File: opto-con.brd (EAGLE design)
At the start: 13 x 8 mm, 2 parts

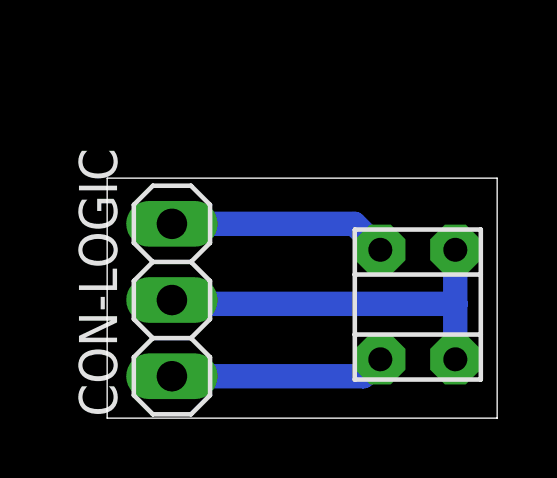
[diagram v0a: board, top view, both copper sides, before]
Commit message: Write meaning of measure signals to silkscreen.
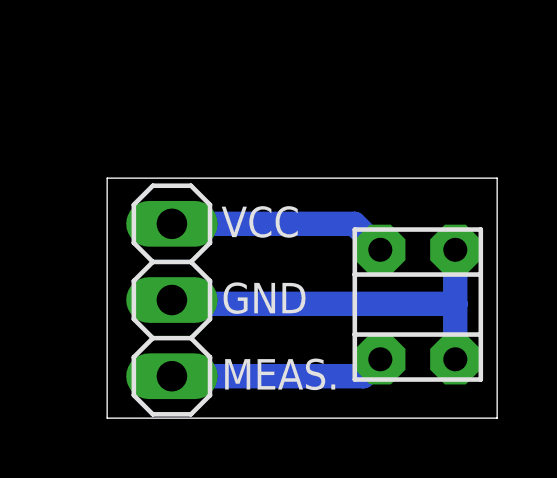
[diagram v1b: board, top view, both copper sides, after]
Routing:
- net GND: track 13.1 -> 13.7 mm
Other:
- board text added: "GND"
- board text added: "MEAS."
- board text added: "VCC"
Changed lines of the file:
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@@
 <grid distance="1.27" unitdist="mm" unit="mm" style="dots" multiple="2" display="no" altdistance="0.3175" altunitdist="mm" altunit="mm"/>
 <layers>
-<layer number="1" name="Top" color="3" fill="1" visible="yes" active="yes"/>
+<layer number="1" name="Top" color="3" fill="1" visible="no" active="yes"/>
 <layer number="2" name="Route2" color="1" fill="3" visible="no" active="no"/>
 <layer number="3" name="Route3" color="4" fill="3" visible="no" active="no"/>
@@
 <layer number="19" name="Unrouted" color="6" fill="1" visible="yes" active="yes"/>
 <layer number="20" name="Dimension" color="24" fill="1" visible="yes" active="yes"/>
-<layer number="21" name="tPlace" color="7" fill="1" visible="yes" active="yes"/>
+<layer number="21" name="tPlace" color="7" fill="1" visible="no" active="yes"/>
 <layer number="22" name="bPlace" color="7" fill="1" visible="yes" active="yes"/>
-<layer number="23" name="tOrigins" color="15" fill="1" visible="yes" active="yes"/>
+<layer number="23" name="tOrigins" color="15" fill="1" visible="no" active="yes"/>
 <layer number="24" name="bOrigins" color="15" fill="1" visible="yes" active="yes"/>
 <layer number="25" name="tNames" color="7" fill="1" visible="no" active="yes"/>
-<layer number="26" name="bNames" color="7" fill="1" visible="no" active="yes"/>
+<layer number="26" name="bNames" color="7" fill="1" visible="yes" active="yes"/>
 <layer number="27" name="tValues" color="7" fill="1" visible="no" active="yes"/>
 <layer number="28" name="bValues" color="7" fill="1" visible="no" active="yes"/>
@@
 <layer number="44" name="Drills" color="7" fill="1" visible="no" active="yes"/>
 <layer number="45" name="Holes" color="7" fill="1" visible="no" active="yes"/>
-<layer number="46" name="Milling" color="3" fill="1" visible="yes" active="yes"/>
+<layer number="46" name="Milling" color="3" fill="1" visible="no" active="yes"/>
 <layer number="47" name="Measures" color="7" fill="1" visible="no" active="yes"/>
 <layer number="48" name="Document" color="7" fill="1" visible="no" active="yes"/>
-<layer number="49" name="Reference" color="7" fill="1" visible="yes" active="yes"/>
-<layer number="51" name="tDocu" color="7" fill="1" visible="yes" active="yes"/>
+<layer number="49" name="Reference" color="7" fill="1" visible="no" active="yes"/>
+<layer number="51" name="tDocu" color="7" fill="1" visible="no" active="yes"/>
 <layer number="52" name="bDocu" color="7" fill="1" visible="yes" active="yes"/>
 <layer number="53" name="tGND_GNDA" color="7" fill="9" visible="no" active="no"/>
@@
 <wire x1="13" y1="8" x2="0" y2="8" width="0" layer="20"/>
 <wire x1="0" y1="8" x2="0" y2="0" width="0" layer="20"/>
+<text x="3.81" y="6.0325" size="1.016" layer="25">VCC</text>
+<text x="3.81" y="0.9525" size="1.016" layer="25">MEAS.</text>
+<text x="3.81" y="3.4925" size="1.016" layer="25">GND</text>
+<text x="3.81" y="6.985" size="1.016" layer="26" rot="MR180">VCC</text>
+<text x="3.81" y="1.905" size="1.016" layer="26" rot="MR180">MEAS.</text>
+<text x="3.81" y="4.445" size="1.016" layer="26" rot="MR180">GND</text>
 </plain>
 <attributes>
@@
 </autorouter>
 <elements>
-<element name="CON-LOGIC" library="pinhead" package="1X03" value="PINHEAD" x="2.159" y="3.937" rot="R90"/>
+<element name="CON-LOGIC" library="pinhead" package="1X03" value="PINHEAD" x="2.159" y="3.937" smashed="yes" rot="R90">
+<attribute name="VALUE" x="5.334" y="0.127" size="1.27" layer="27" rot="R90"/>
+</element>
 <element name="OP1" library="optosensor" package="GP1S23" value="GP1S23" x="8.255" y="6.2865" smashed="yes" rot="R270"/>
 </elements>
@@
 <wire x1="11.605" y1="5.6115" x2="11.605" y2="3.81" width="0.8128" layer="16"/>
 <wire x1="11.605" y1="3.81" x2="11.605" y2="1.9615" width="0.8128" layer="16"/>
-<wire x1="2.159" y1="3.937" x2="2.286" y2="3.81" width="0.8128" layer="16"/>
+<wire x1="2.159" y1="3.937" x2="2.413" y2="3.937" width="0.8128" layer="16"/>
+<wire x1="2.413" y1="3.937" x2="2.54" y2="3.81" width="0.8128" layer="16"/>
+<wire x1="2.54" y1="3.81" x2="2.286" y2="3.81" width="0.8128" layer="16"/>
 <wire x1="2.286" y1="3.81" x2="11.605" y2="3.81" width="0.8128" layer="16"/>
 </signal>
